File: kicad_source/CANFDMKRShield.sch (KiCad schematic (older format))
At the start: 30 parts, among them CN1 ARDUINO_MKR, CN2 CONN_01X04, CN3 GH_SM04B-GHS-TB, CN4 GH_SM04B-GHS-TB, SW1 JS202011JCQN, U1 MCP2517FD, U2 SN65HVD232, U3 TPS54232, Y1 20MHz

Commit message: added diode D2 to connect CAN VCC to 5V
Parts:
- added D2: DNI, diodes:SOD-123, symbol devices:D_Schottky_Small
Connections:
- net labels added: CANVCC
- wire segments 125 -> 126
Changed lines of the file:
@@
 Sheet 1 1
 Title "CANFDMKRShield"
-Date "2020-11-25"
+Date "2020-11-27"
 Rev "0.1"
 Comp "generationmake"
@@
 	1    0    0    -1
 $EndComp
-$Comp
-L power-supply:+5V #PWR0103
-U 1 1 5FBF104E
-P 9950 1150
-F 0 "#PWR0103" H 9950 1000 50  0001 C CNN
-F 1 "+5V" H 9965 1323 50  0000 C CNN
-F 2 "" H 9950 1150 50  0000 C CNN
-F 3 "" H 9950 1150 50  0000 C CNN
-	1    9950 1150
-	1    0    0    -1
-$EndComp
-Wire Wire Line
-	10050 1250 9950 1250
-Wire Wire Line
-	9950 1250 9950 1150
 Wire Wire Line
 	10050 1550 9950 1550
@@
 	1    0    0    -1
 $EndComp
-$Comp
-L power-supply:+5V #PWR0105
-U 1 1 5FBFC4EB
-P 9950 2100
-F 0 "#PWR0105" H 9950 1950 50  0001 C CNN
-F 1 "+5V" H 9965 2273 50  0000 C CNN
-F 2 "" H 9950 2100 50  0000 C CNN
-F 3 "" H 9950 2100 50  0000 C CNN
-	1    9950 2100
-	1    0    0    -1
-$EndComp
-Wire Wire Line
-	10050 2200 9950 2200
-Wire Wire Line
-	9950 2200 9950 2100
 Wire Wire Line
 	10050 2500 9950 2500
@@
 Text Notes 9300 2100 0    50   ~ 0
 CAN out
+$Comp
+L devices:D_Schottky_Small D2
+U 1 1 5FC0AD4A
+P 9450 3350
+F 0 "D2" H 9450 3555 50  0000 C CNN
+F 1 "DNI" H 9450 3464 50  0000 C CNN
+F 2 "diodes:SOD-123" V 9450 3350 50  0001 C CNN
+F 3 "" V 9450 3350 50  0000 C CNN
+	1    9450 3350
+	1    0    0    -1
+$EndComp
+$Comp
+L power-supply:+5V #PWR027
+U 1 1 5FC0BA56
+P 9200 3300
+F 0 "#PWR027" H 9200 3150 50  0001 C CNN
+F 1 "+5V" H 9215 3473 50  0000 C CNN
+F 2 "" H 9200 3300 50  0000 C CNN
+F 3 "" H 9200 3300 50  0000 C CNN
+	1    9200 3300
+	1    0    0    -1
+$EndComp
+Wire Wire Line
+	10250 3350 9550 3350
+Wire Wire Line
+	9350 3350 9200 3350
+Wire Wire Line
+	9200 3350 9200 3300
+Text Label 9350 2200 0    50   ~ 0
+CANVCC
+Text Label 9350 1250 0    50   ~ 0
+CANVCC
+Text Label 9800 3350 0    50   ~ 0
+CANVCC
+Wire Wire Line
+	9200 2200 10050 2200
+Wire Wire Line
+	9200 1250 10050 1250
 $EndSCHEMATC

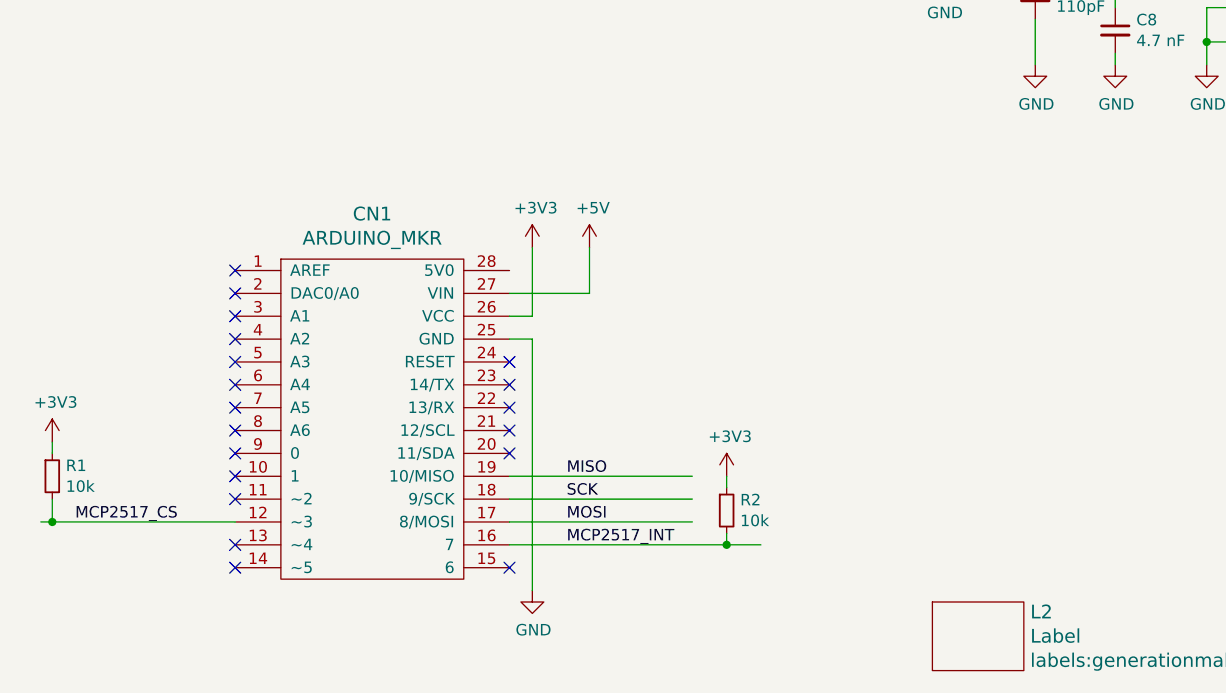
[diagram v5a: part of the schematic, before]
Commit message: added option to use different CS line for SPI
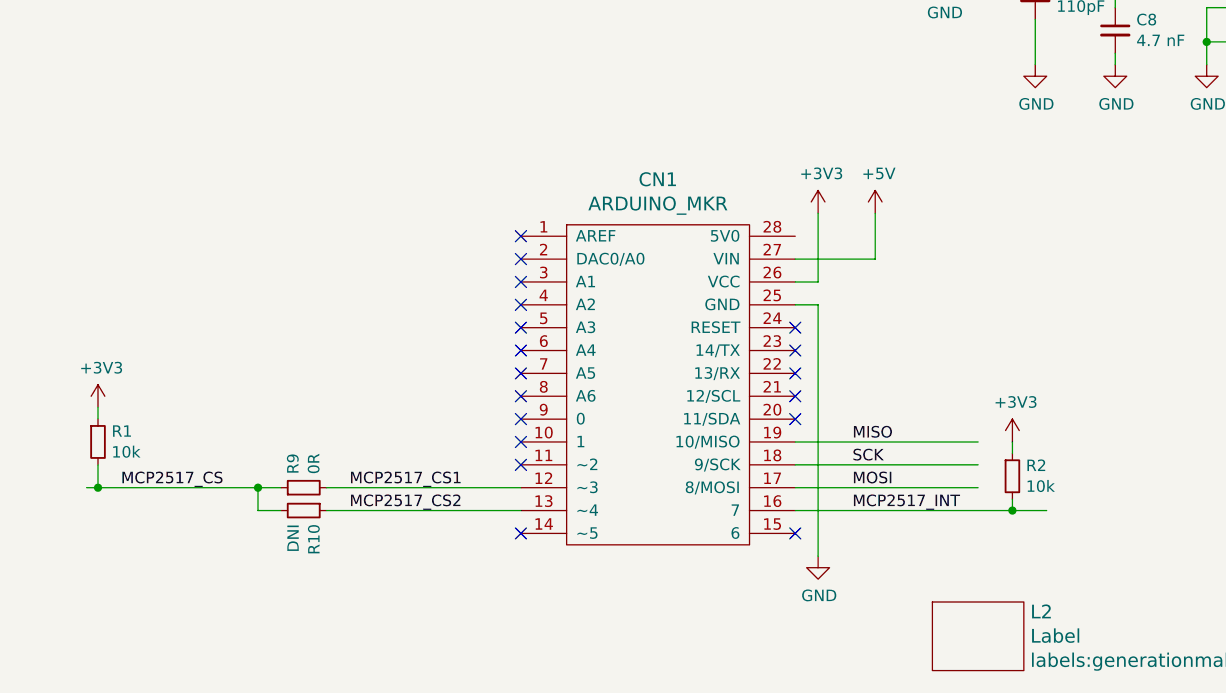
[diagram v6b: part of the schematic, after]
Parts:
- added R10: DNI, resistors:R_0603, symbol devices:R_0603
- added R9: 0R, resistors:R_0603, symbol devices:R_0603
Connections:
- net labels added: MCP2517_CS1, MCP2517_CS2
- wire segments 126 -> 131
- no-connect marks 25 -> 24
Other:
- moved on the sheet: CN1, R1, R2
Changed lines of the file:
@@
 L MODULE_compute:ARDUINO_MKR CN1
 U 1 1 5FB0F5B4
-P 2350 6650
-F 0 "CN1" H 2350 7547 60  0000 C CNN
-F 1 "ARDUINO_MKR" H 2350 7441 60  0000 C CNN
-F 2 "MODULE_compute:ARDUINO_MKR_HOLES_PINHEADER_EDGE" H 2250 7300 60  0001 C CNN
-F 3 "" H 2350 6350 60  0000 C CNN
-	1    2350 6650
+P 3600 6500
+F 0 "CN1" H 3600 7397 60  0000 C CNN
+F 1 "ARDUINO_MKR" H 3600 7291 60  0000 C CNN
+F 2 "MODULE_compute:ARDUINO_MKR_HOLES_PINHEADER_EDGE" H 3500 7150 60  0001 C CNN
+F 3 "" H 3600 6200 60  0000 C CNN
+	1    3600 6500
 	1    0    0    -1
 $EndComp
@@
 L power-supply:+3V3 #PWR02
 U 1 1 5FB1D8E4
-P 3050 5900
-F 0 "#PWR02" H 3050 5750 50  0001 C CNN
-F 1 "+3V3" H 3065 6073 50  0000 C CNN
-F 2 "" H 3050 5900 50  0000 C CNN
-F 3 "" H 3050 5900 50  0000 C CNN
-	1    3050 5900
+P 4300 5750
+F 0 "#PWR02" H 4300 5600 50  0001 C CNN
+F 1 "+3V3" H 4315 5923 50  0000 C CNN
+F 2 "" H 4300 5750 50  0000 C CNN
+F 3 "" H 4300 5750 50  0000 C CNN
+	1    4300 5750
 	1    0    0    -1
 $EndComp
@@
 L power-supply:GND #PWR03
 U 1 1 5FB1E67A
-P 3050 7400
-F 0 "#PWR03" H 3050 7150 50  0001 C CNN
-F 1 "GND" H 3055 7227 50  0000 C CNN
-F 2 "" H 3050 7400 50  0000 C CNN
-F 3 "" H 3050 7400 50  0000 C CNN
-	1    3050 7400
-	1    0    0    -1
-$EndComp
-Wire Wire Line
-	2950 6300 3050 6300
-Wire Wire Line
-	3050 6300 3050 7400
-Wire Wire Line
-	2950 6200 3050 6200
-Wire Wire Line
-	3050 6200 3050 5900
-NoConn ~ 2950 6400
-NoConn ~ 2950 6500
-NoConn ~ 2950 6600
-NoConn ~ 2950 6700
-NoConn ~ 2950 6800
-NoConn ~ 2950 7300
-Wire Wire Line
-	3750 6900 2950 6900
-Wire Wire Line
-	3750 7000 2950 7000
-Wire Wire Line
-	3750 7100 2950 7100
-Text Label 3200 7000 0    50   ~ 0
+P 4300 7250
+F 0 "#PWR03" H 4300 7000 50  0001 C CNN
+F 1 "GND" H 4305 7077 50  0000 C CNN
+F 2 "" H 4300 7250 50  0000 C CNN
+F 3 "" H 4300 7250 50  0000 C CNN
+	1    4300 7250
+	1    0    0    -1
+$EndComp
+Wire Wire Line
+	4200 6150 4300 6150
+Wire Wire Line
+	4300 6150 4300 7250
+Wire Wire Line
+	4200 6050 4300 6050
+Wire Wire Line
+	4300 6050 4300 5750
+NoConn ~ 4200 6250
+NoConn ~ 4200 6350
+NoConn ~ 4200 6450
+NoConn ~ 4200 6550
+NoConn ~ 4200 6650
+NoConn ~ 4200 7150
+Wire Wire Line
+	5000 6750 4200 6750
+Wire Wire Line
+	5000 6850 4200 6850
+Wire Wire Line
+	5000 6950 4200 6950
+Text Label 4450 6850 0    50   ~ 0
 SCK
-Text Label 3200 7100 0    50   ~ 0
+Text Label 4450 6950 0    50   ~ 0
 MOSI
-Text Label 3200 6900 0    50   ~ 0
+Text Label 4450 6750 0    50   ~ 0
 MISO
 Wire Wire Line
-	900  7100 950  7100
-Text Label 1050 7100 0    50   ~ 0
+	1100 6950 1150 6950
+Text Label 1250 6950 0    50   ~ 0
 MCP2517_CS
 Wire Wire Line
-	2950 7200 3900 7200
-Text Label 3200 7200 0    50   ~ 0
+	4200 7050 5150 7050
+Text Label 4450 7050 0    50   ~ 0
 MCP2517_INT
 $Comp
 L devices:R_0603 R2
 U 1 1 5FB2791D
-P 3900 7050
-F 0 "R2" H 3959 7096 50  0000 L CNN
-F 1 "10k" H 3959 7005 50  0000 L CNN
-F 2 "resistors:R_0603" H 3900 6900 50  0001 C CNN
-F 3 "" H 3900 7050 50  0000 C CNN
-	1    3900 7050
+P 5150 6900
+F 0 "R2" H 5209 6946 50  0000 L CNN
+F 1 "10k" H 5209 6855 50  0000 L CNN
+F 2 "resistors:R_0603" H 5150 6750 50  0001 C CNN
+F 3 "" H 5150 6900 50  0000 C CNN
+	1    5150 6900
 	1    0    0    -1
 $EndComp
@@
 L power-supply:+3V3 #PWR05
 U 1 1 5FB2889D
-P 3900 6900
-F 0 "#PWR05" H 3900 6750 50  0001 C CNN
-F 1 "+3V3" H 3915 7073 50  0000 C CNN
-F 2 "" H 3900 6900 50  0000 C CNN
-F 3 "" H 3900 6900 50  0000 C CNN
-	1    3900 6900
-	1    0    0    -1
-$EndComp
-Wire Wire Line
-	3900 6900 3900 6950
-Wire Wire Line
-	3900 7150 3900 7200
-Connection ~ 3900 7200
-Wire Wire Line
-	3900 7200 4050 7200
+P 5150 6750
+F 0 "#PWR05" H 5150 6600 50  0001 C CNN
+F 1 "+3V3" H 5165 6923 50  0000 C CNN
+F 2 "" H 5150 6750 50  0000 C CNN
+F 3 "" H 5150 6750 50  0000 C CNN
+	1    5150 6750
+	1    0    0    -1
+$EndComp
+Wire Wire Line
+	5150 6750 5150 6800
+Wire Wire Line
+	5150 7000 5150 7050
+Connection ~ 5150 7050
+Wire Wire Line
+	5150 7050 5300 7050
 $Comp
 L devices:R_0603 R1
 U 1 1 5FB2AA84
-P 950 6900
-F 0 "R1" H 1009 6946 50  0000 L CNN
-F 1 "10k" H 1009 6855 50  0000 L CNN
-F 2 "resistors:R_0603" H 950 6750 50  0001 C CNN
-F 3 "" H 950 6900 50  0000 C CNN
-	1    950  6900
+P 1150 6750
+F 0 "R1" H 1209 6796 50  0000 L CNN
+F 1 "10k" H 1209 6705 50  0000 L CNN
+F 2 "resistors:R_0603" H 1150 6600 50  0001 C CNN
+F 3 "" H 1150 6750 50  0000 C CNN
+	1    1150 6750
 	1    0    0    -1
 $EndComp
@@
 L power-supply:+3V3 #PWR01
 U 1 1 5FB2AB46
-P 950 6750
-F 0 "#PWR01" H 950 6600 50  0001 C CNN
-F 1 "+3V3" H 965 6923 50  0000 C CNN
-F 2 "" H 950 6750 50  0000 C CNN
-F 3 "" H 950 6750 50  0000 C CNN
-	1    950  6750
-	1    0    0    -1
-$EndComp
-Wire Wire Line
-	950  6750 950  6800
-Wire Wire Line
-	950  7000 950  7100
-Connection ~ 950  7100
-Wire Wire Line
-	950  7100 1750 7100
-NoConn ~ 1750 6000
-NoConn ~ 1750 6100
-NoConn ~ 1750 6200
-NoConn ~ 1750 6300
-NoConn ~ 1750 6400
-NoConn ~ 1750 6500
-NoConn ~ 1750 6600
-NoConn ~ 1750 6700
-NoConn ~ 1750 6800
-NoConn ~ 1750 6900
-NoConn ~ 1750 7000
-NoConn ~ 1750 7200
-NoConn ~ 1750 7300
+P 1150 6600
+F 0 "#PWR01" H 1150 6450 50  0001 C CNN
+F 1 "+3V3" H 1165 6773 50  0000 C CNN
+F 2 "" H 1150 6600 50  0000 C CNN
+F 3 "" H 1150 6600 50  0000 C CNN
+	1    1150 6600
+	1    0    0    -1
+$EndComp
+Wire Wire Line
+	1150 6600 1150 6650
+Wire Wire Line
+	1150 6850 1150 6950
+Connection ~ 1150 6950
+Wire Wire Line
+	1150 6950 1850 6950
+NoConn ~ 3000 5850
+NoConn ~ 3000 5950
+NoConn ~ 3000 6050
+NoConn ~ 3000 6150
+NoConn ~ 3000 6250
+NoConn ~ 3000 6350
+NoConn ~ 3000 6450
+NoConn ~ 3000 6550
+NoConn ~ 3000 6650
+NoConn ~ 3000 6750
+NoConn ~ 3000 6850
+NoConn ~ 3000 7150
 $Comp
 L CAN-transceiver:SN65HVD232 U2
@@
 L power-supply:+5V #PWR0101
 U 1 1 5FBCFCC0
-P 3300 5900
-F 0 "#PWR0101" H 3300 5750 50  0001 C CNN
-F 1 "+5V" H 3315 6073 50  0000 C CNN
-F 2 "" H 3300 5900 50  0000 C CNN
-F 3 "" H 3300 5900 50  0000 C CNN
-	1    3300 5900
-	1    0    0    -1
-$EndComp
-Wire Wire Line
-	2950 6100 3300 6100
-Wire Wire Line
-	3300 6100 3300 5900
+P 4550 5750
+F 0 "#PWR0101" H 4550 5600 50  0001 C CNN
+F 1 "+5V" H 4565 5923 50  0000 C CNN
+F 2 "" H 4550 5750 50  0000 C CNN
+F 3 "" H 4550 5750 50  0000 C CNN
+	1    4550 5750
+	1    0    0    -1
+$EndComp
+Wire Wire Line
+	4200 5950 4550 5950
+Wire Wire Line
+	4550 5950 4550 5750
 $Comp
 L devices:Label L2
@@
 Wire Wire Line
 	9200 1250 10050 1250
+$Comp
+L devices:R_0603 R9
+U 1 1 5FC1AD02
+P 2050 6950
+F 0 "R9" H 2109 6996 50  0000 L CNN
+F 1 "0R" H 2109 6905 50  0000 L CNN
+F 2 "resistors:R_0603" H 2050 6800 50  0001 C CNN
+F 3 "" H 2050 6950 50  0000 C CNN
+	1    2050 6950
+	0    -1   -1   0
+$EndComp
+$Comp
+L devices:R_0603 R10
+U 1 1 5FC1B795
+P 2050 7050
+F 0 "R10" H 2109 7096 50  0000 L CNN
+F 1 "DNI" H 2109 7005 50  0000 L CNN
+F 2 "resistors:R_0603" H 2050 6900 50  0001 C CNN
+F 3 "" H 2050 7050 50  0000 C CNN
+	1    2050 7050
+	0    1    1    0
+$EndComp
+Wire Wire Line
+	1950 7050 1850 7050
+Wire Wire Line
+	1850 7050 1850 6950
+Connection ~ 1850 6950
+Wire Wire Line
+	1850 6950 1950 6950
+Wire Wire Line
+	2150 6950 3000 6950
+Wire Wire Line
+	3000 7050 2150 7050
+Text Label 2250 6950 0    50   ~ 0
+MCP2517_CS1
+Text Label 2250 7050 0    50   ~ 0
+MCP2517_CS2
 $EndSCHEMATC

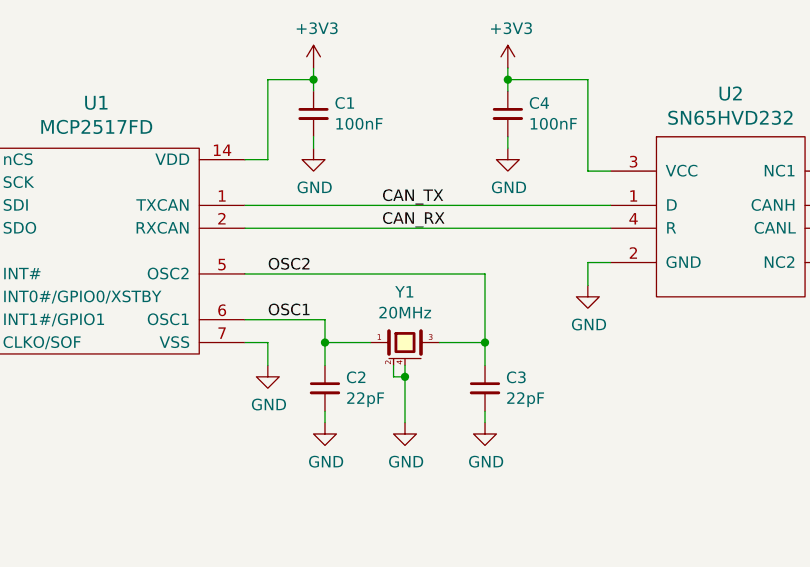
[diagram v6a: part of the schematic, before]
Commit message: defined type of crystal, updated 3d models of footprints
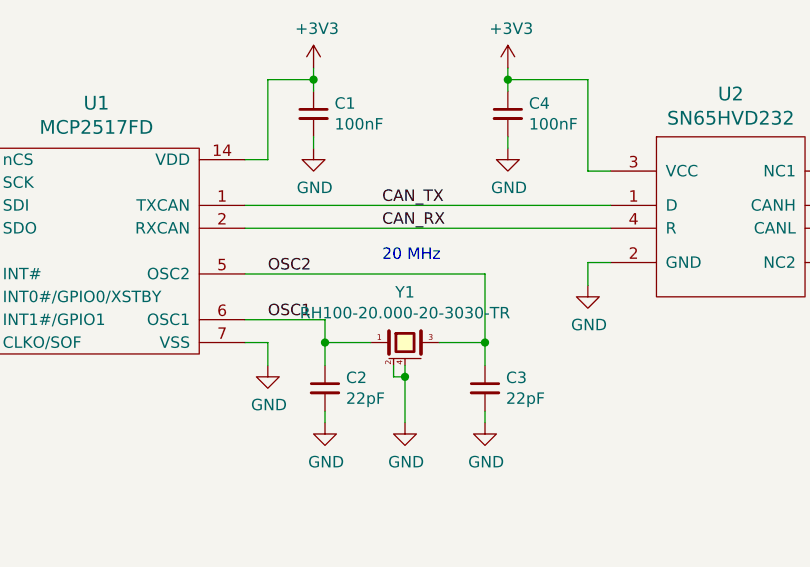
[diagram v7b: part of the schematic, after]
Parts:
- Y1: value 20MHz -> RH100-20.000-20-3030-TR; footprint crystals:Crystal_SMD_0603_4Pads -> crystals:Crystal_SMD_3.2x2.5mm_4Pad
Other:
- note added: "20 MHz"
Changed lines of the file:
@@
 P 3500 2150
 F 0 "Y1" H 3500 2370 50  0000 C CNN
-F 1 "20MHz" H 3500 2279 50  0000 C CNN
-F 2 "crystals:Crystal_SMD_0603_4Pads" H 3500 1950 50  0001 C CNN
+F 1 "RH100-20.000-20-3030-TR" H 3500 2279 50  0000 C CNN
+F 2 "crystals:Crystal_SMD_3.2x2.5mm_4Pad" H 3500 1950 50  0001 C CNN
 F 3 "" H 3500 2150 50  0000 C CNN
 	1    3500 2150
@@
 Text Label 2250 7050 0    50   ~ 0
 MCP2517_CS2
+Text Notes 3400 1800 0    50   ~ 0
+20 MHz
 $EndSCHEMATC

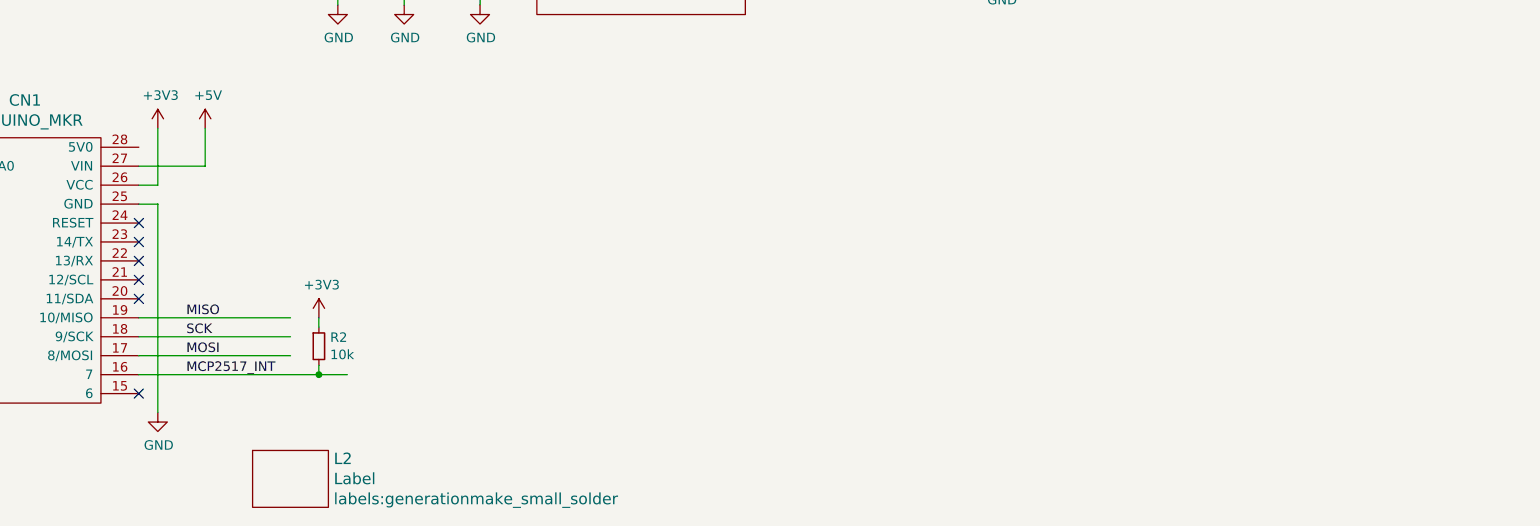
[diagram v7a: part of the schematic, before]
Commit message: added some labels, updated images and schematic pdf
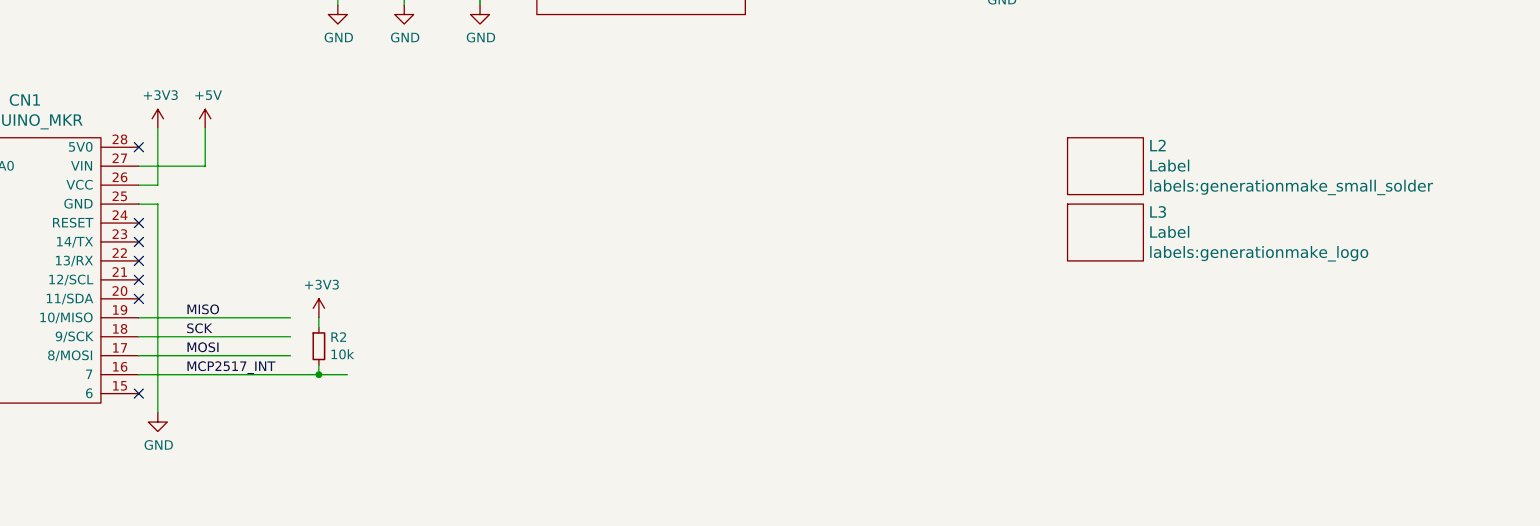
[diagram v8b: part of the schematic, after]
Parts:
- added L3: Label, labels:generationmake_logo, symbol devices:Label
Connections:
- no-connect marks 24 -> 25
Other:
- moved on the sheet: L2
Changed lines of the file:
@@
 Sheet 1 1
 Title "CANFDMKRShield"
-Date "2020-11-27"
+Date "2020-11-28"
 Rev "0.1"
 Comp "generationmake"
@@
 L devices:Label L2
 U 1 1 5FBD8ED2
-P 5000 7600
-F 0 "L2" H 5228 7706 60  0000 L CNN
-F 1 "Label" H 5228 7600 60  0000 L CNN
-F 2 "labels:generationmake_small_solder" H 5228 7494 60  0000 L CNN
-F 3 "" H 5000 7600 60  0000 C CNN
-	1    5000 7600
+P 9300 5950
+F 0 "L2" H 9528 6056 60  0000 L CNN
+F 1 "Label" H 9528 5950 60  0000 L CNN
+F 2 "labels:generationmake_small_solder" H 9528 5844 60  0000 L CNN
+F 3 "" H 9300 5950 60  0000 C CNN
+	1    9300 5950
 	1    0    0    -1
 $EndComp
@@
 Text Notes 3400 1800 0    50   ~ 0
 20 MHz
+$Comp
+L devices:Label L3
+U 1 1 5FC37959
+P 9300 6300
+F 0 "L3" H 9528 6406 60  0000 L CNN
+F 1 "Label" H 9528 6300 60  0000 L CNN
+F 2 "labels:generationmake_logo" H 9528 6194 60  0000 L CNN
+F 3 "" H 9300 6300 60  0000 C CNN
+	1    9300 6300
+	1    0    0    -1
+$EndComp
+NoConn ~ 4200 5850
 $EndSCHEMATC
